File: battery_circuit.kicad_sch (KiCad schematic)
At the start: 18 parts, among them IC1 BQ24040DSQR, IC2 BQ27441DRZR-G1A, J2 Conn_01x06, J3 Molex-PicoBlade

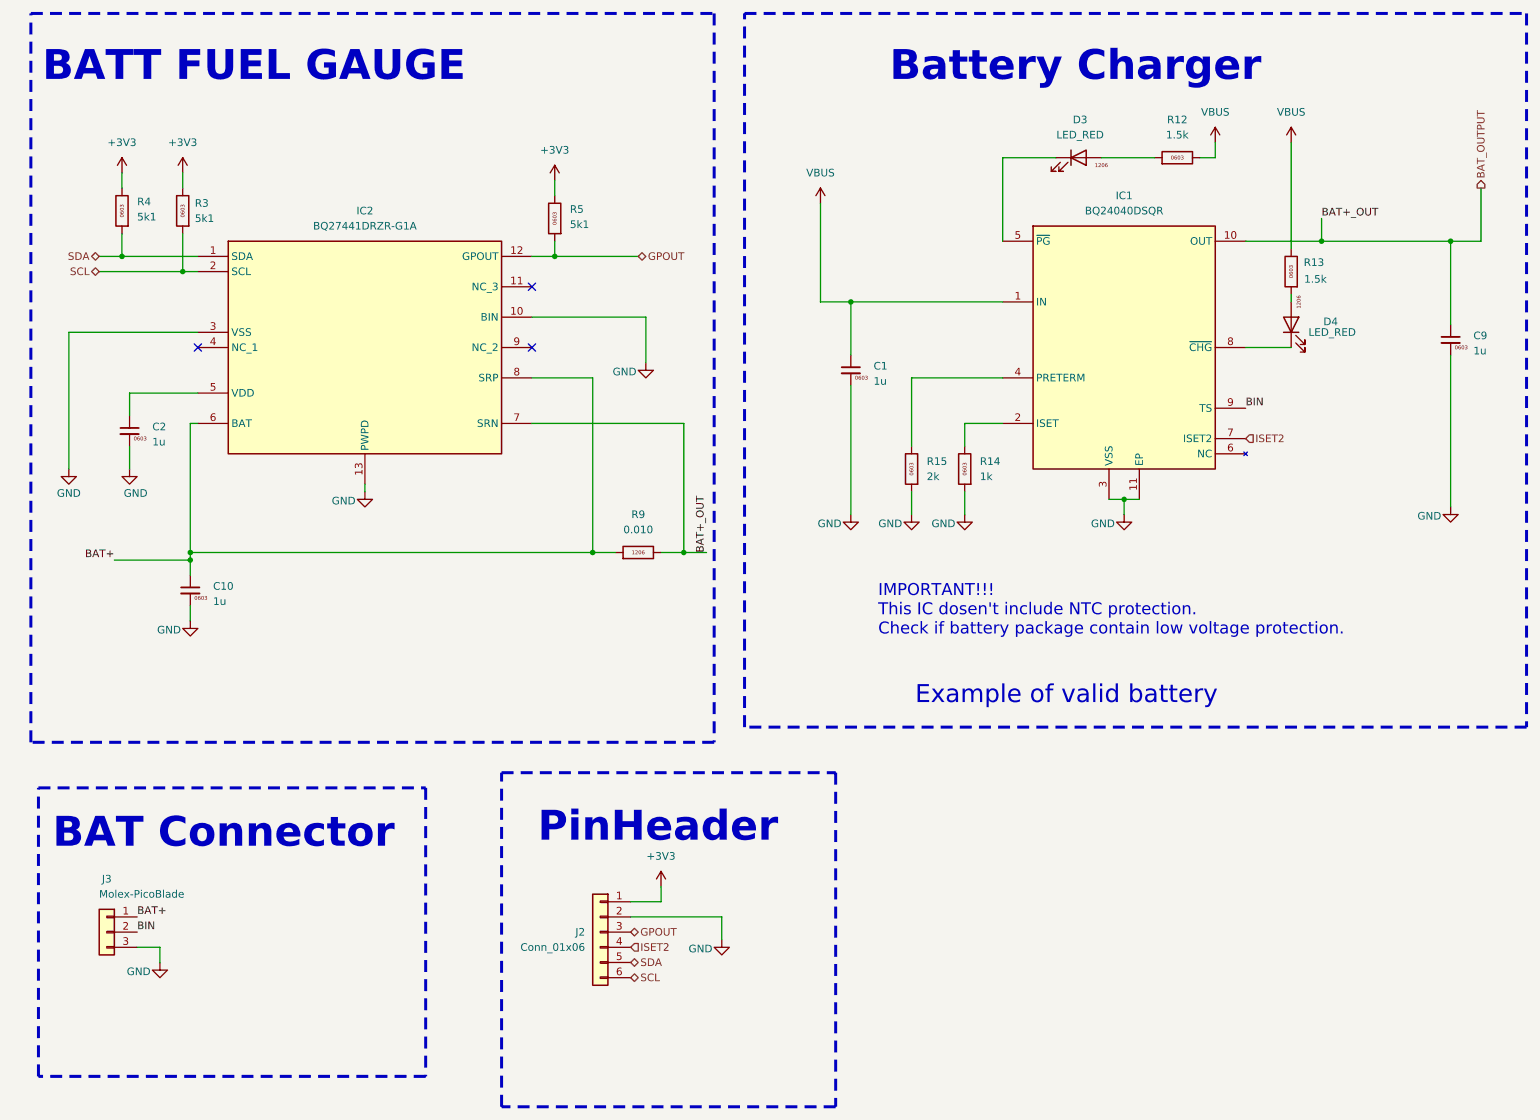
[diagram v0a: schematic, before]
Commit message: fix: Buck Converter inductor changed to the right type
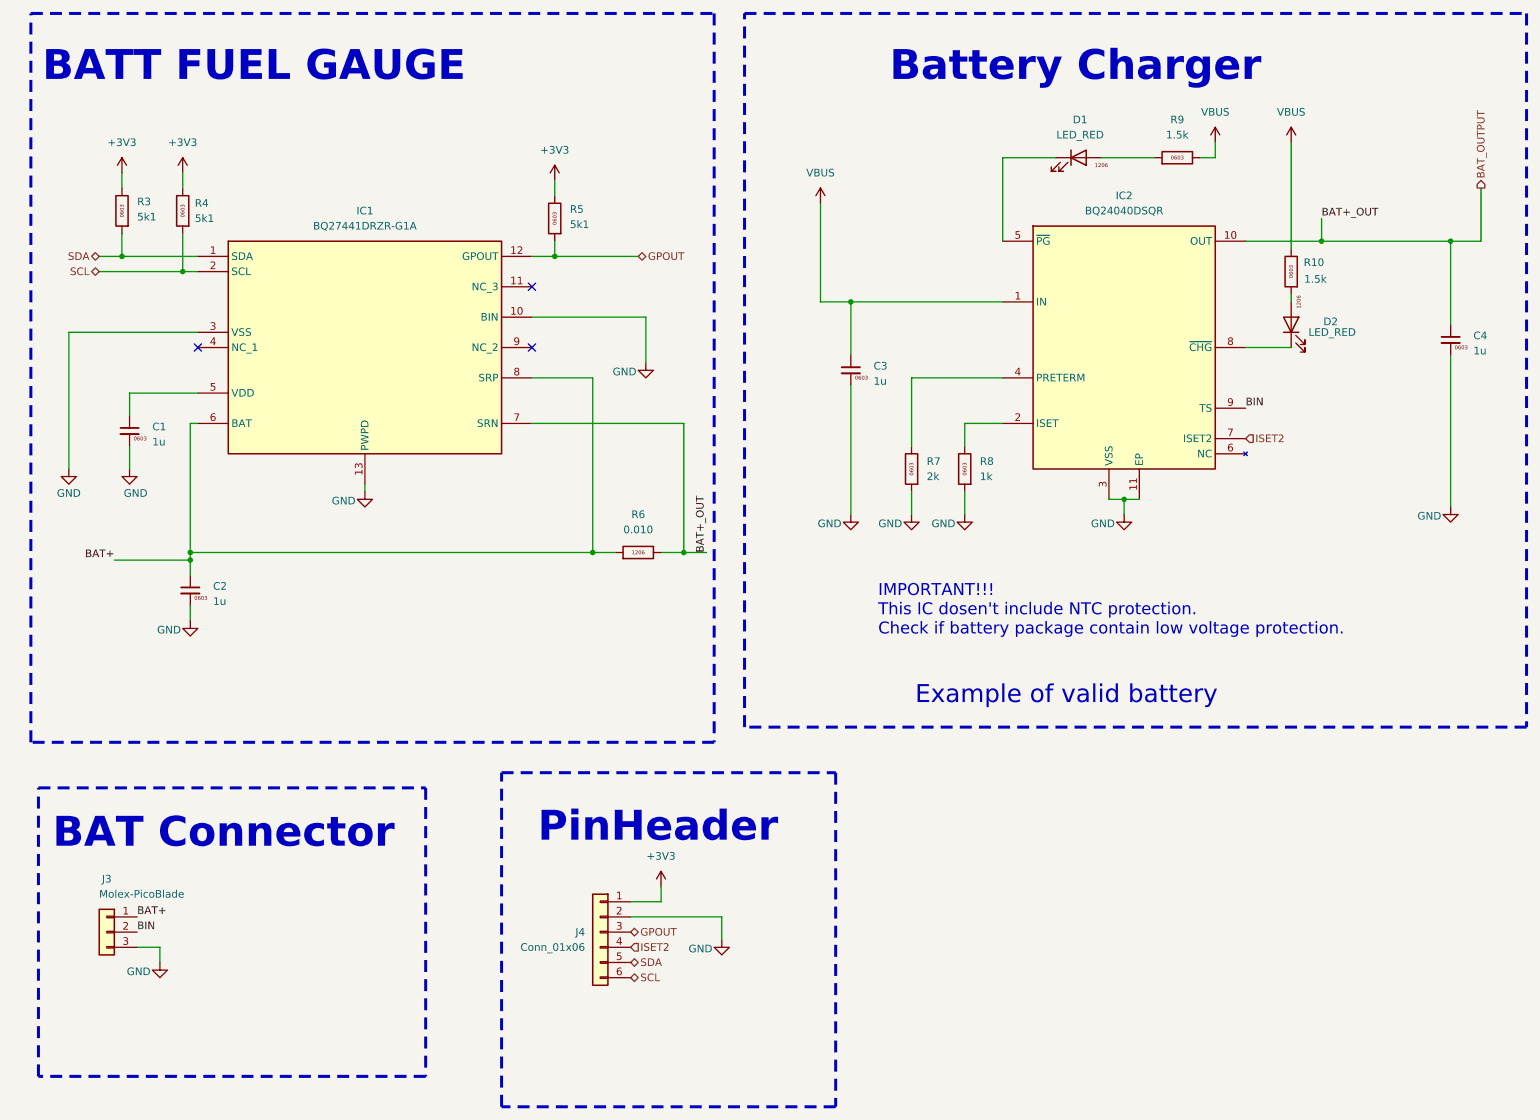
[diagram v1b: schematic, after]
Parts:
- renumbered C2 to C1, C10 to C2, C1 to C3, C9 to C4, D3 to D1, D4 to D2, IC2 to IC1, IC1 to IC2, J2 to J4, R13 to R10, R4 to R3, R3 to R4, R9 to R6, R15 to R7, R14 to R8, R12 to R9
